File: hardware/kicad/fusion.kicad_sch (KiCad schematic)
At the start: 32 parts, among them J1 BATTERY, J2 LSM6DSOX, J3 PICKIT, J4 HC-05, J5 FLEX, J7 FTDI, SW1 BUTTON, SW2 POWER, SW3 UART, U1 MCP1603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

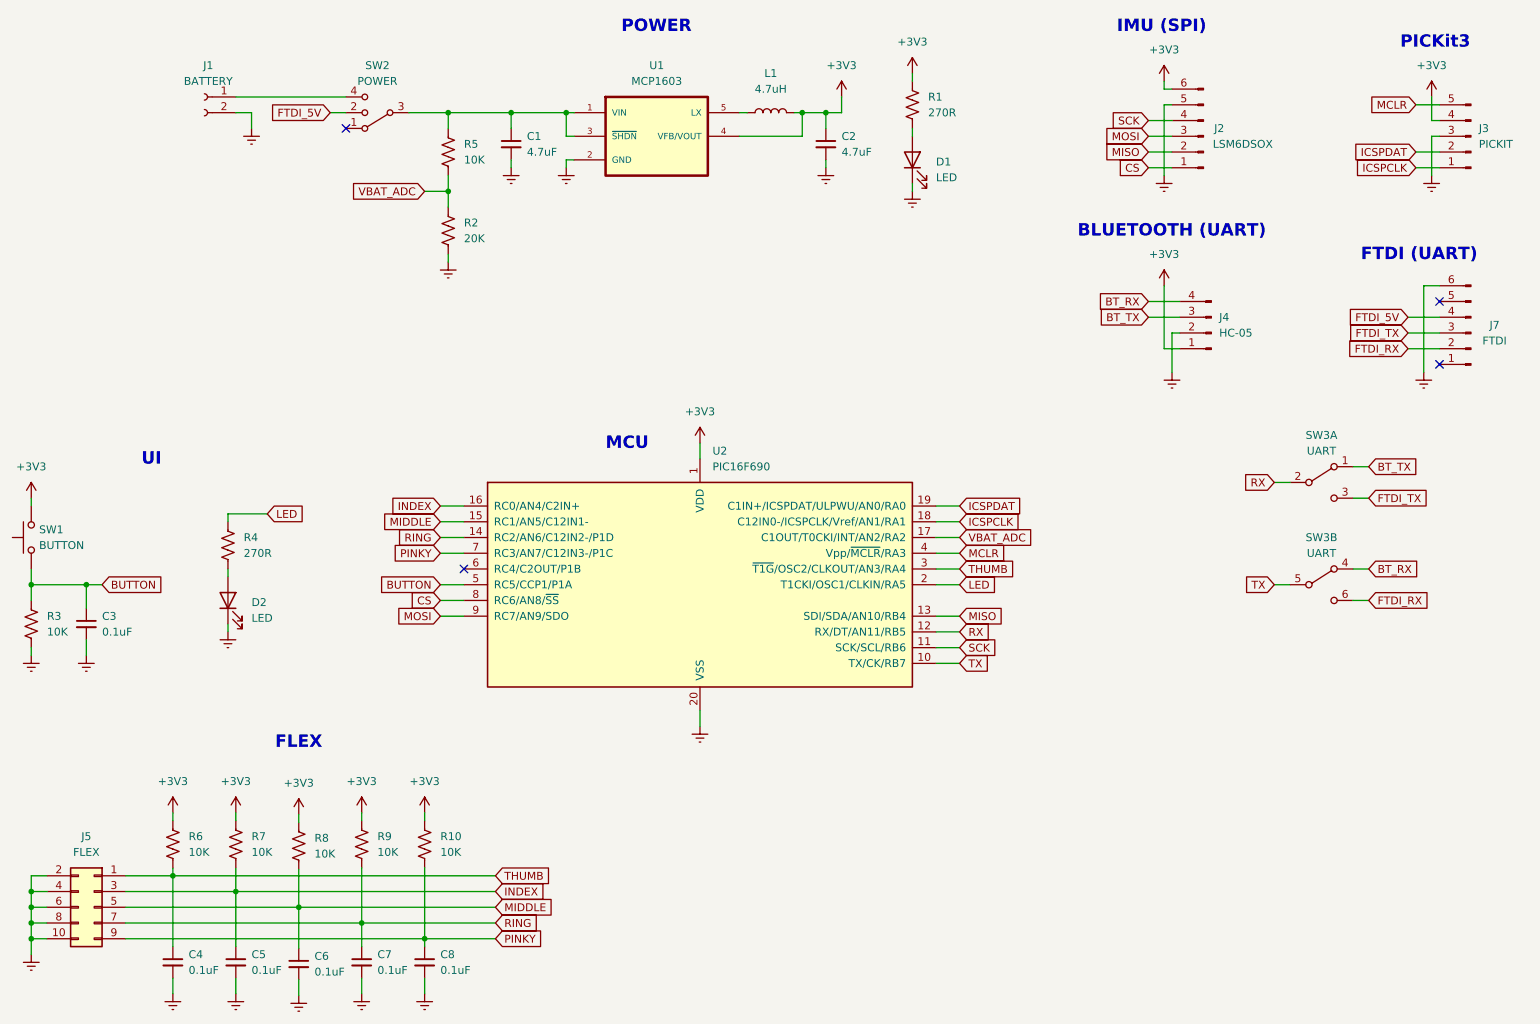
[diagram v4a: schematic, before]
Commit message: Rename FTDI to USB
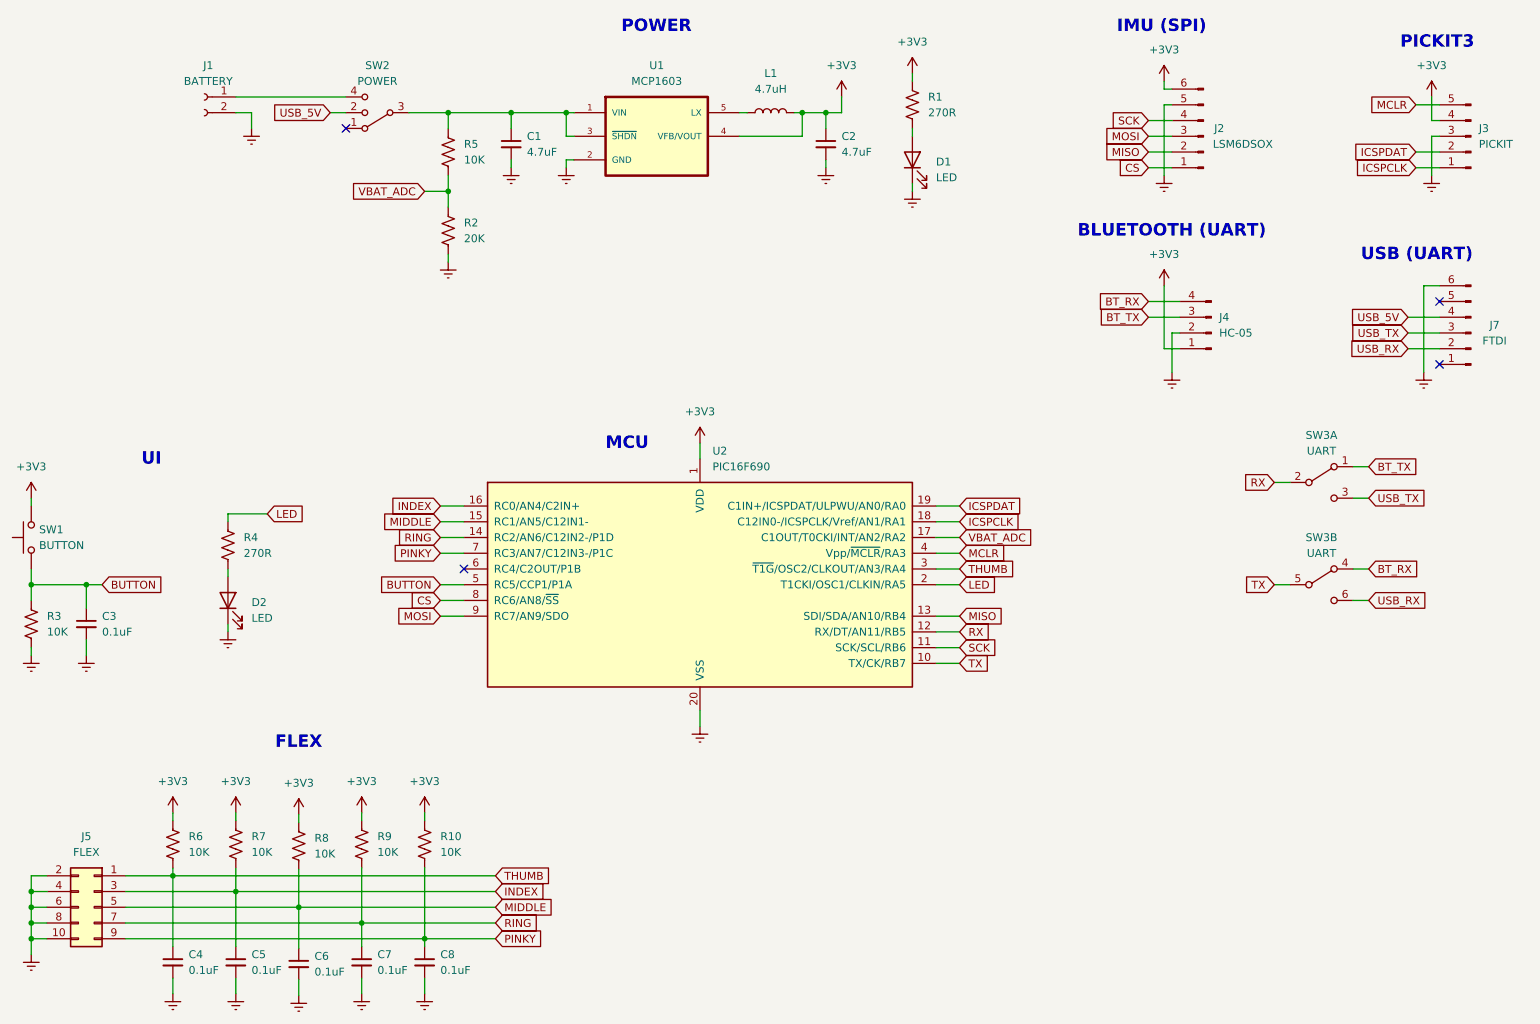
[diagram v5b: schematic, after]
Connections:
- net FTDI_5V renamed USB_5V
- net FTDI_RX renamed USB_RX
- net FTDI_TX renamed USB_TX
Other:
- note added: "PICKIT3"
- note added: "USB (UART)"
- note removed: "FTDI (UART)"
- note removed: "PICKit3"
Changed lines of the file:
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@@
     (effects (font (size 2 2) (thickness 0.254) bold) (justify left bottom))
   )
-  (text "PICKit3" (at 247.65 27.94 0)
-    (effects (font (size 2 2) (thickness 0.254) bold) (justify left bottom))
-  )
-  (text "FTDI (UART)" (at 241.3 62.23 0)
+  (text "PICKIT3" (at 247.65 27.94 0)
+    (effects (font (size 2 2) (thickness 0.254) bold) (justify left bottom))
+  )
+  (text "USB (UART)" (at 241.3 62.23 0)
     (effects (font (size 2 2) (thickness 0.254) bold) (justify left bottom))
   )
@@
     )
   )
-  (global_label "FTDI_RX" (shape input) (at 248.92 76.2 180) (fields_autoplaced)
-    (effects (font (size 1.27 1.27)) (justify right))
-    (property "Intersheet References" "${INTERSHEET_REFS}" (id 0) (at 239.1288 76.1206 0)
+  (global_label "USB_RX" (shape input) (at 248.92 76.2 180) (fields_autoplaced)
+    (effects (font (size 1.27 1.27)) (justify right))
+    (property "Intersheet References" "${INTERSHEET_REFS}" (id 0) (at 239.2498 76.1206 0)
       (effects (font (size 1.27 1.27)) (justify right) hide)
     )
@@
     )
   )
-  (global_label "FTDI_RX" (shape input) (at 242.57 116.84 0) (fields_autoplaced)
-    (effects (font (size 1.27 1.27)) (justify left))
-    (property "Intersheet References" "${INTERSHEET_REFS}" (id 0) (at 252.3612 116.7606 0)
+  (global_label "USB_RX" (shape input) (at 242.57 116.84 0) (fields_autoplaced)
+    (effects (font (size 1.27 1.27)) (justify left))
+    (property "Intersheet References" "${INTERSHEET_REFS}" (id 0) (at 252.2402 116.7606 0)
       (effects (font (size 1.27 1.27)) (justify left) hide)
     )
@@
     )
   )
-  (global_label "FTDI_TX" (shape input) (at 248.92 73.66 180) (fields_autoplaced)
-    (effects (font (size 1.27 1.27)) (justify right))
-    (property "Intersheet References" "${INTERSHEET_REFS}" (id 0) (at 239.4312 73.5806 0)
+  (global_label "USB_TX" (shape input) (at 248.92 73.66 180) (fields_autoplaced)
+    (effects (font (size 1.27 1.27)) (justify right))
+    (property "Intersheet References" "${INTERSHEET_REFS}" (id 0) (at 239.5521 73.5806 0)
       (effects (font (size 1.27 1.27)) (justify right) hide)
     )
@@
     )
   )
-  (global_label "FTDI_TX" (shape input) (at 242.57 100.33 0) (fields_autoplaced)
-    (effects (font (size 1.27 1.27)) (justify left))
-    (property "Intersheet References" "${INTERSHEET_REFS}" (id 0) (at 252.0588 100.2506 0)
+  (global_label "USB_TX" (shape input) (at 242.57 100.33 0) (fields_autoplaced)
+    (effects (font (size 1.27 1.27)) (justify left))
+    (property "Intersheet References" "${INTERSHEET_REFS}" (id 0) (at 251.9379 100.2506 0)
       (effects (font (size 1.27 1.27)) (justify left) hide)
     )
@@
     )
   )
-  (global_label "FTDI_5V" (shape input) (at 74.93 38.1 180) (fields_autoplaced)
-    (effects (font (size 1.27 1.27)) (justify right))
-    (property "Intersheet References" "${INTERSHEET_REFS}" (id 0) (at 65.3202 38.0206 0)
+  (global_label "USB_5V" (shape input) (at 74.93 38.1 180) (fields_autoplaced)
+    (effects (font (size 1.27 1.27)) (justify right))
+    (property "Intersheet References" "${INTERSHEET_REFS}" (id 0) (at 65.4412 38.0206 0)
       (effects (font (size 1.27 1.27)) (justify right) hide)
     )
@@
     )
   )
-  (global_label "FTDI_5V" (shape input) (at 248.92 71.12 180) (fields_autoplaced)
-    (effects (font (size 1.27 1.27)) (justify right))
-    (property "Intersheet References" "${INTERSHEET_REFS}" (id 0) (at 239.3102 71.0406 0)
-      (effects (font (size 1.27 1.27)) (justify right) hide)
-    )
+  (global_label "USB_5V" (shape input) (at 248.92 71.12 180) (fields_autoplaced)
+    (effects (font (size 1.27 1.27)) (justify right))
+    (property "Intersheet References" "${INTERSHEET_REFS}" (id 0) (at 239.4312 71.0406 0)
+      (effects (font (size 1.27 1.27)) (justify right) hide)
+    )
